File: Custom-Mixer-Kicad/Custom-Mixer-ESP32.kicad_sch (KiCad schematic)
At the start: 28 parts, among them J1 OLED1, J2 OLED2, J3 OLED3, J4 OLED4, J5 OLED5, J6 TCA9548A, SW1 RotaryEncoder_Switch, SW2 RotaryEncoder_Switch, U1 ESP32-DevKitC

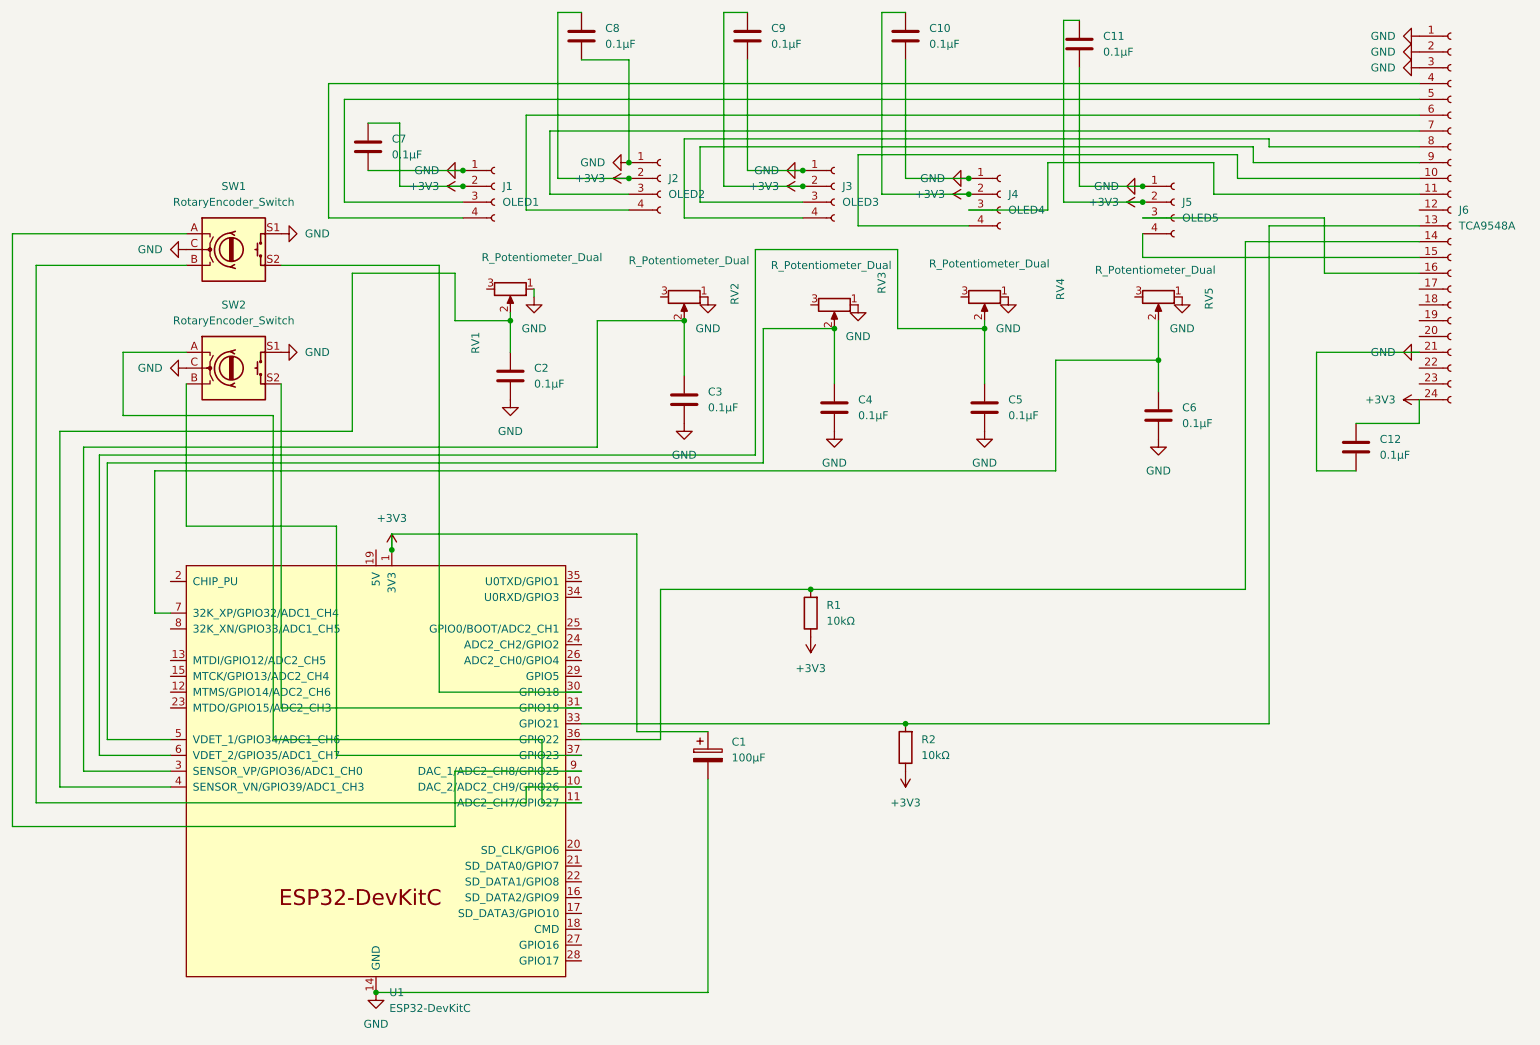
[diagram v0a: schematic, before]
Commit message: Redo File directory and 2nd revision of PCB and schematic
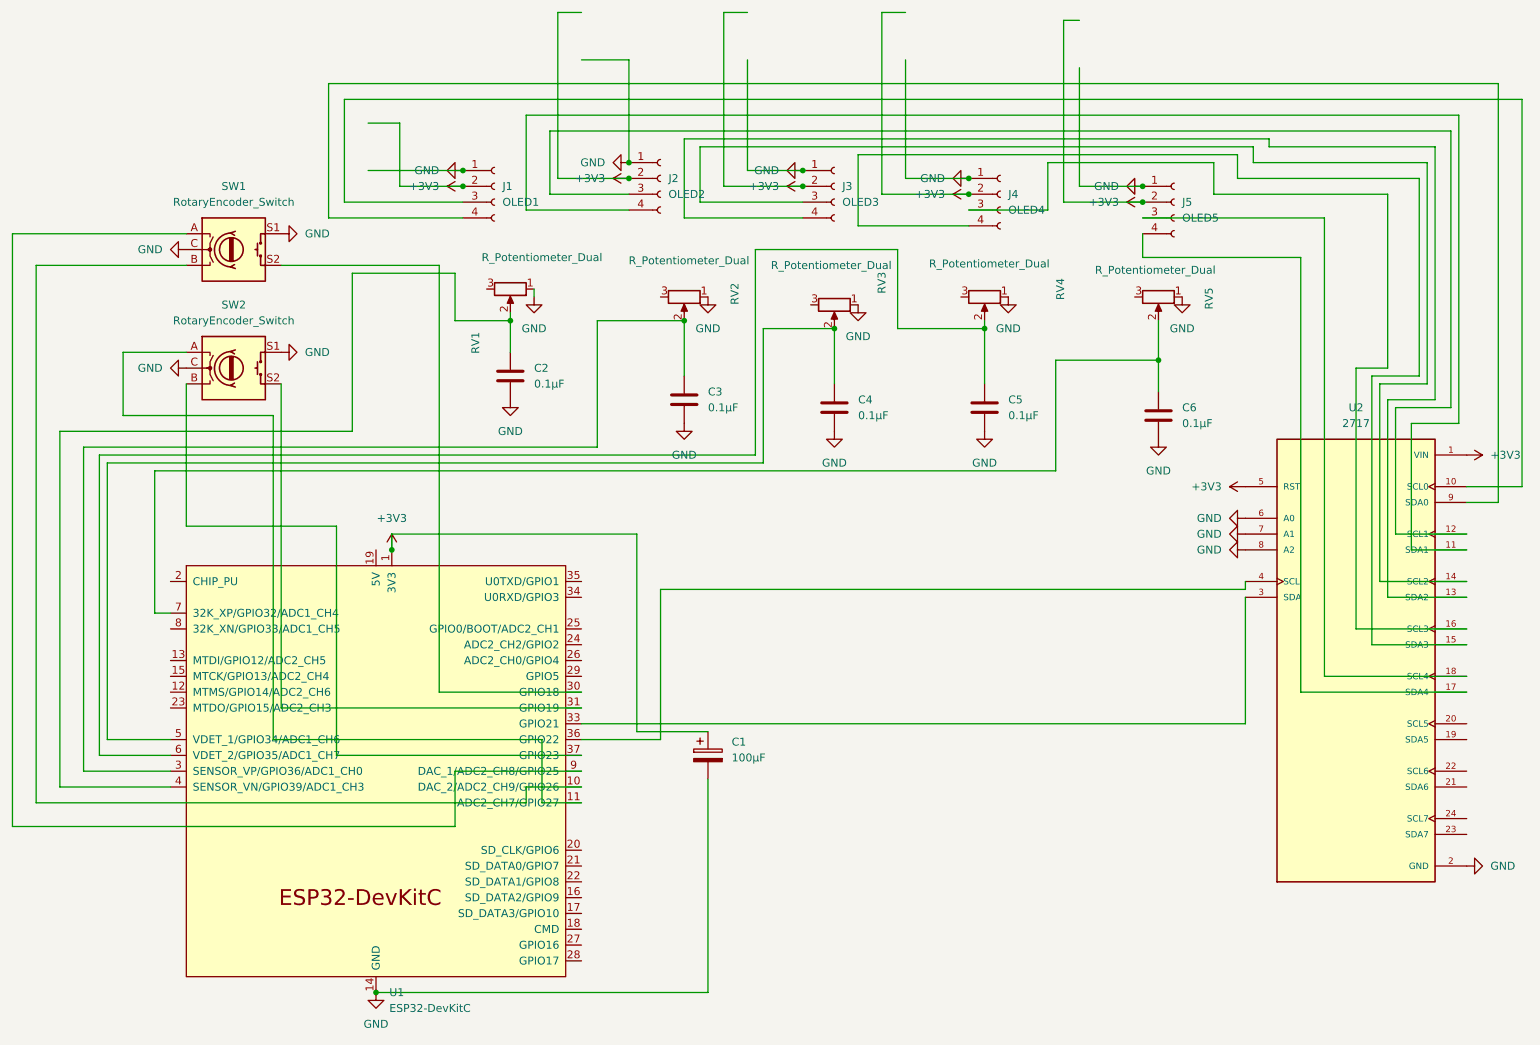
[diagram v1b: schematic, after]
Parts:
- removed C10, C11, C12, C7, C8, C9: 0.1µF, Capacitor_THT:C_Disc_D5.0mm_W2.5mm_P2.50mm, symbol Device:C
- removed J6: TCA9548A, TCA9548A Breakout:MODULE_2717, symbol Connector:Conn_01x24_Socket
- removed R1, R2: 10kΩ, Resistor_THT:R_Axial_DIN0207_L6.3mm_D2.5mm_P10.16mm_Horizontal, symbol Device:R
- added U2: 2717, TCA9548A Breakout:MODULE_2717, symbol 2717:2717
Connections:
- net +3V3: now also U2.1 (VIN), U2.5 (RST)
- net GND: now also U2.2 (GND), U2.6 (A0), U2.7 (A1), U2.8 (A2)
- net at U1.33 (GPIO21): now also U2.3 (SDA)
- net at J3.3 (Pin_3): now also U2.14 (SCL2)
- net at J3.4 (Pin_4): now also U2.13 (SDA2)
- net at J1.3 (Pin_3): now also U2.10 (SCL0)
- net at J1.4 (Pin_4): now also U2.9 (SDA0)
- net at J4.3 (Pin_3): now also U2.16 (SCL3)
- net at J4.4 (Pin_4): now also U2.15 (SDA3)
- net at U1.36 (GPIO22): now also U2.4 (SCL)
- net at J2.3 (Pin_3): now also U2.12 (SCL1)
- net at J2.4 (Pin_4): now also U2.11 (SDA1)
- net at J5.3 (Pin_3): now also U2.18 (SCL4)
- net at J5.4 (Pin_4): now also U2.17 (SDA4)
